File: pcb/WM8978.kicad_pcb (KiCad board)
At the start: 2 copper layers, 7.7 x 1.7 mm, 50 parts, among them CN2 HEADPHONE 3.5mm, SW4 RESET, U15 AMS1117-3.3, U16 WM8978GEFL/RV, U17 STM32F407VET6, X3 8MHz CL=12pF

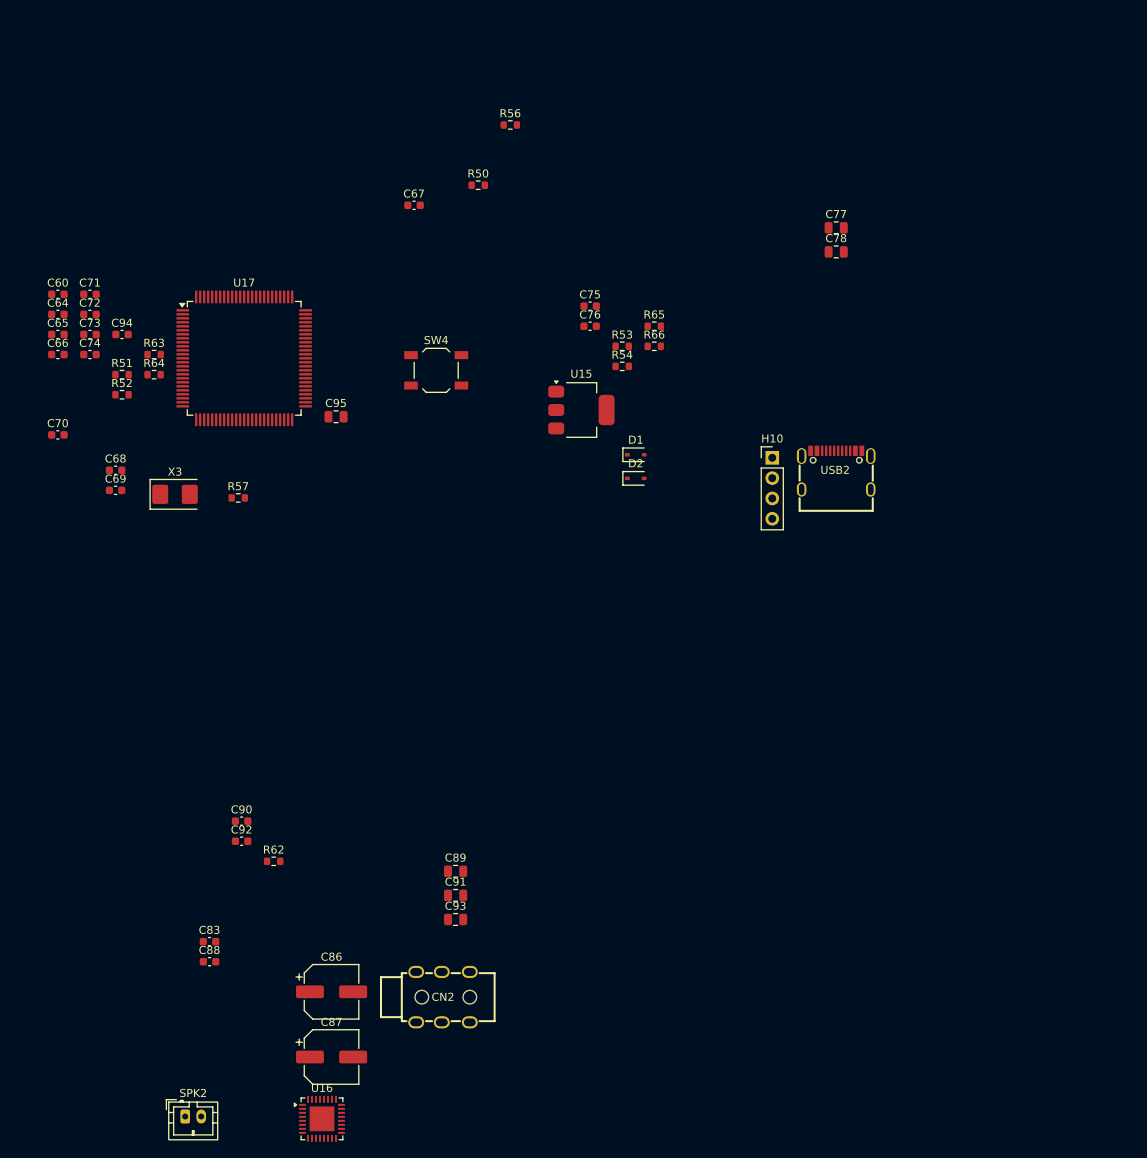
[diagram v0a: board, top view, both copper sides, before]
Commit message: 修复原理图电源网络并更新项目文档
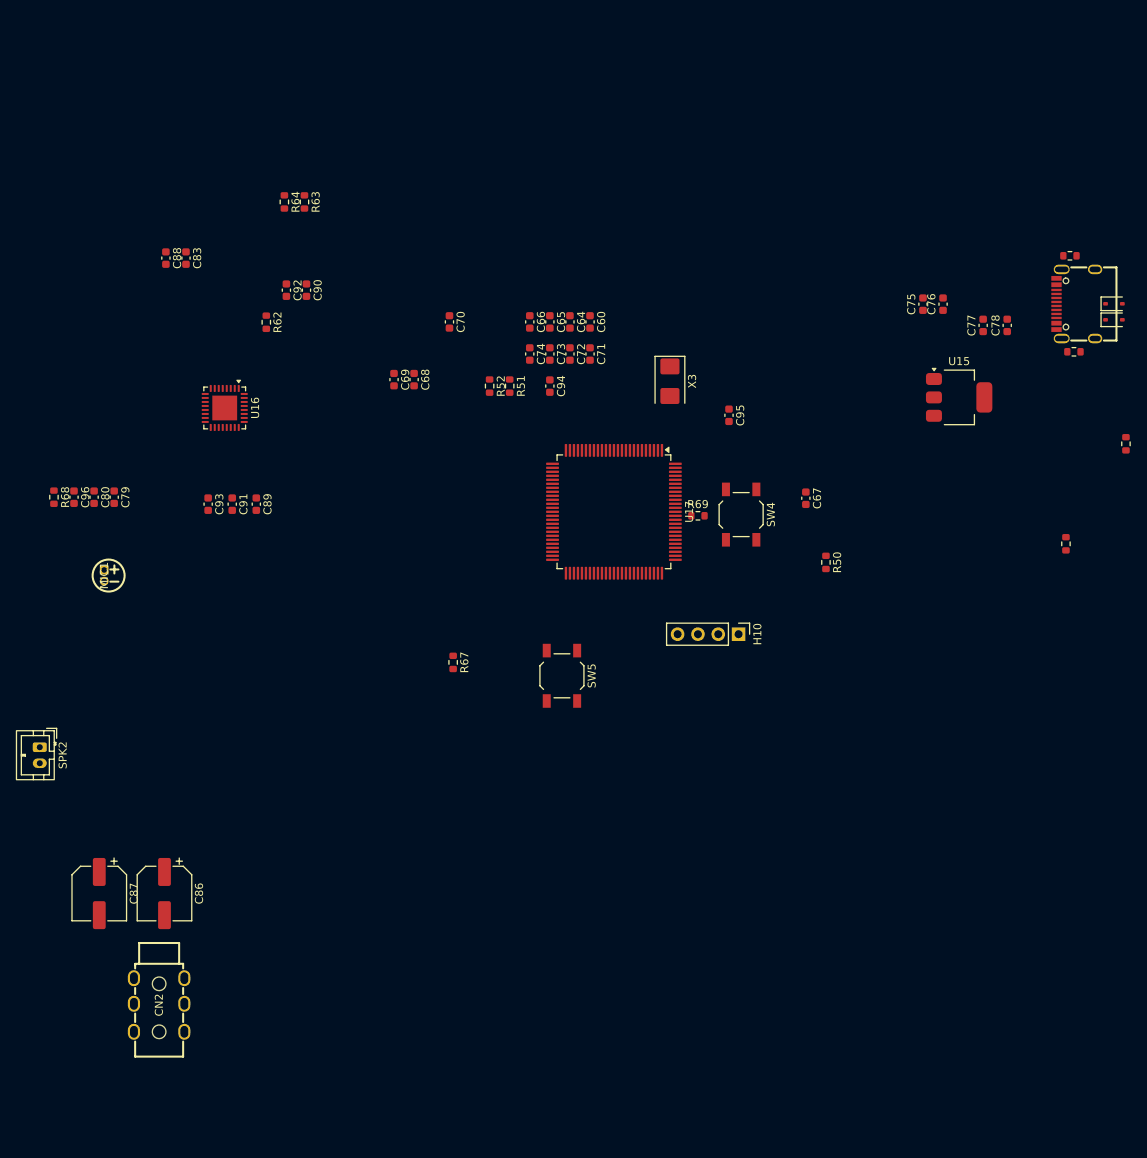
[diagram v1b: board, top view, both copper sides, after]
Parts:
- removed R56: 10k, Resistor_SMD:R_0603_1608Metric
- removed R57: 1M, Resistor_SMD:R_0603_1608Metric
- added C79: 1uF, Capacitor_SMD:C_0603_1608Metric, F.Cu at (90.0, 89.7)
- added C80: 1uF, Capacitor_SMD:C_0603_1608Metric, F.Cu at (87.5, 89.7)
- added C96: 4.7uF, Capacitor_SMD:C_0603_1608Metric, F.Cu at (85.0, 89.7)
- added MIC1: ELECTRET MIC, WM8978-import-fps:MIC-TH_BD4.0-P1.40-D0.4-L-FD, F.Cu at (88.8, 99.5)
- added R67: 1k, Resistor_SMD:R_0603_1608Metric, F.Cu at (132.4, 110.3)
- added R68: 2.2k, Resistor_SMD:R_0603_1608Metric, F.Cu at (82.5, 89.7)
- added R69: 10k, Resistor_SMD:R_0603_1608Metric, F.Cu at (163.0, 92.0)
- added SW5: BOOT, Button_Switch_SMD:SW_SPST_TL3342, F.Cu at (146.0, 112.0)
- C77, C89, C91, C93: value 10uF -> 4.7uF; footprint Capacitor_SMD:C_0805_2012Metric -> Capacitor_SMD:C_0603_1608Metric
- C78: footprint Capacitor_SMD:C_0805_2012Metric -> Capacitor_SMD:C_0603_1608Metric
- C86, C87: value 220uF/6.3V -> 220uF/16V
- C95: value 4.7uF -> 100nF; footprint Capacitor_SMD:C_0805_2012Metric -> Capacitor_SMD:C_0603_1608Metric
- U15: value AMS1117-3.3 -> TLV1117LV33DCYR
- moved U16 89.7 mm to (103.8, 78.5), turned to -90 degrees
- moved C88 88.1 mm to (96.5, 59.8), turned to -90 degrees
- moved C83 85.5 mm to (99.0, 59.8), turned to -90 degrees
- moved C92 69.1 mm to (111.6, 63.8), turned to -90 degrees
- moved R62 67.4 mm to (109.0, 67.8), turned to -90 degrees
- moved C90 66.9 mm to (114.1, 63.8), turned to -90 degrees
- moved C60 66.6 mm to (149.5, 67.8), turned to -90 degrees
- moved R53 64.1 mm to (216.5, 83.0), turned to 90 degrees
- moved R50 64.1 mm to (179.0, 97.8), turned to -90 degrees
- moved C64 64.0 mm to (147.0, 67.8), turned to -90 degrees
- moved X3 63.5 mm to (159.5, 75.2), turned to -90 degrees
- moved D2 63.0 mm to (215.0, 67.5)
- moved C71 63.0 mm to (149.5, 71.8), turned to -90 degrees
- moved D1 62.7 mm to (215.0, 65.5)
- moved C65 61.5 mm to (144.5, 67.8), turned to -90 degrees
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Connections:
- net /BOOT0 renamed Net-(U17A-BOOT0)
- net /CC1 renamed Net-(USB2-CC1)
- net /CC2 renamed Net-(USB2-CC2)
- net /LOUT2 renamed /SPK_N
- net /NRST renamed Net-(U17A-NRST)
- net /OS_IN renamed Net-(U17A-PH0-OSC_IN(PH0))
- net /OS_OUT renamed Net-(U17A-PH1-OSC_OUT(PH1))
- net /PA11 renamed /USB_DM
- net /PA12 renamed /USB_DP
- net /PA13 renamed Net-(U17A-PA13(JTMS-SWDIO))
- net /PA14 renamed Net-(U17A-PA14(JTCK-SWCLK))
- net /ROUT2 renamed /SPK_P
- net /USB_DM_CONN renamed Net-(D2-A1)
- net /USB_DP_CONN renamed Net-(D1-A1)
- net /VSSA renamed Net-(U17B-VSSA)
- net Net-(U16-MODE) renamed /MODE
- C60 pad 1: /VDDA -> /GND
- C60 pad 2: GND -> /VDDA
- C64 pad 1: GND -> /GND
- C65 pad 2: GND -> /GND
- C66 pad 2: GND -> /GND
- C67 pad 1: GND -> /GND
- C68 pad 2: GND -> /GND
- C69 pad 2: GND -> /GND
- C70 pad 1: VCC3V3 -> /3V3
- C70 pad 2: GND -> /GND
- C71 pad 1: VCC3V3 -> /3V3
- C71 pad 2: GND -> /GND
- C72 pad 1: VCC3V3 -> /3V3
- C72 pad 2: GND -> /GND
- C73 pad 1: VCC3V3 -> /3V3
- C73 pad 2: GND -> /GND
- C74 pad 1: VCC3V3 -> /3V3
- C74 pad 2: GND -> /GND
- C75 pad 1: GND -> /VBUS_5V
- C75 pad 2: +5V -> /GND
- C76 pad 1: GND -> /3V3
- C76 pad 2: VCC3V3 -> /GND
- C77 pad 1: GND -> /VBUS_5V
- C77 pad 2: +5V -> /GND
- C78 pad 1: GND -> /3V3
- C78 pad 2: VCC3V3 -> /GND
- C83 pad 1: GND -> /GND
- C86 pad 1: Net-(U16-ROUT1) -> /HP_L
- C87 pad 1: Net-(U16-LOUT1) -> /HP_R
- C88 pad 1: VCC3V3 -> /3V3
- C88 pad 2: GND -> /GND
- C89 pad 1: GND -> /GND
- C89 pad 2: VCC3V3 -> /3V3
- C90 pad 1: VCC3V3 -> /3V3
- C90 pad 2: GND -> /GND
- C91 pad 1: GND -> /GND
- C91 pad 2: VCC3V3 -> /3V3
- C92 pad 1: +5V -> /GND
- C92 pad 2: GND -> /VBUS_5V
- C93 pad 1: GND -> /VBUS_5V
- C93 pad 2: +5V -> /GND
- C94 pad 1: VCC3V3 -> /3V3
- C94 pad 2: GND -> /GND
- C95 pad 1: VCC3V3 -> /3V3
- C95 pad 2: GND -> /GND
- CN2 pad 2: GND -> /GND
- D1 pad 2: GND -> /GND
- D2 pad 2: GND -> /GND
- H10 pad 1: VCC3V3 -> /3V3
- H10 pad 4: GND -> /GND
- R50 pad 2: GND -> /GND
- R51 pad 2: GND -> /GND
- R52 pad 2: VCC3V3 -> /3V3
- R62 pad 1: GND -> /GND
- R63 pad 1: VCC3V3 -> Net-(U16-SDIN)
- R63 pad 2: /WM8978_SDIN -> /3V3
- R64 pad 1: VCC3V3 -> Net-(U16-SCLK)
- R64 pad 2: /WM8978_SCLK -> /3V3
- R65 pad 2: GND -> /GND
- R66 pad 2: GND -> /GND
- SW4 pad 2: GND -> /GND
- U15 pad 1: GND -> /GND
- U15 pad 2: VCC3V3 -> /3V3
- U15 pad 3: +5V -> /VBUS_5V
- U15 pad 4: VCC3V3 -> /3V3
- U16 pad 1: unconnected-(U16-LIP-Pad1) -> /MIC_LIP
- U16 pad 12: GND -> /GND
- U16 pad 13: VCC3V3 -> /GND
- U16 pad 14: VCC3V3 -> /3V3
- U16 pad 15: GND -> /GND
- U16 pad 16: /WM8978_SCLK -> Net-(U16-SCLK)
- U16 pad 17: /WM8978_SDIN -> Net-(U16-SDIN)
- U16 pad 2: unconnected-(U16-LIN-Pad2) -> /MIC_LIN
- U16 pad 24: GND -> /GND
- U16 pad 26: +5V -> /VBUS_5V
- U16 pad 28: GND -> /GND
- U16 pad 29: Net-(U16-ROUT1) -> /HP_R
- U16 pad 30: Net-(U16-LOUT1) -> /HP_L
- U16 pad 31: VCC3V3 -> /GND
- U16 pad 32: unconnected-(U16-MICBIAS-Pad32) -> Net-(U16-MICBIAS)
- U16 pad 33: GND -> /GND
- U16 pad 9: unconnected-(U16-ADCDAT-Pad9) -> /I2S_ADCDAT
- U17 pad 10: GND -> /GND
- U17 pad 100: VCC3V3 -> /3V3
- U17 pad 11: VCC3V3 -> /3V3
- U17 pad 17: unconnected-(U17A-PC2-Pad17) -> /I2S_ADCDAT
- U17 pad 19: VCC3V3 -> /3V3
- U17 pad 27: GND -> /GND
- U17 pad 28: VCC3V3 -> /3V3
- U17 pad 37: unconnected-(U17A-PB2-BOOT1(PB2)-Pad37) -> Net-(U17A-PB2-BOOT1(PB2))
- U17 pad 50: VCC3V3 -> /3V3
- U17 pad 6: VCC3V3 -> /3V3
- U17 pad 68: unconnected-(U17A-PA9-Pad68) -> Net-(U17A-PA9)
- U17 pad 74: GND -> /GND
- U17 pad 75: VCC3V3 -> /3V3
- U17 pad 87: /WM8978_SCLK -> /CODEC_SCLK
- U17 pad 88: /WM8978_SDIN -> /CODEC_SDIN
- U17 pad 99: GND -> /GND
- USB2 pad 1: GND -> /GND
- USB2 pad 2: GND -> /GND
- USB2 pad 3: GND -> /GND
- USB2 pad 4: GND -> /GND
- USB2 pad A1: GND -> /GND
- USB2 pad A12: GND -> /GND
- USB2 pad A4: +5V -> /VBUS_5V
- USB2 pad A9: +5V -> /VBUS_5V
- USB2 pad B1: GND -> /GND
- USB2 pad B12: GND -> /GND
- USB2 pad B4: +5V -> /VBUS_5V
- USB2 pad B9: +5V -> /VBUS_5V
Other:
- board size 7.7 x 1.7 mm -> 1.7 x 7.7 mm

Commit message: 更新单页原理图布局并同步 PCB
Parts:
- C95: value 100nF -> 4.7uF
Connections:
- C79 pad 1: Net-(C79-Pad1) -> /MIC_LIP
- C79 pad 2: /MIC_LIP -> Net-(C79-Pad2)
- C80 pad 1: /GND -> unconnected-(C80-Pad1)
- C80 pad 2: /MIC_LIN -> unconnected-(C80-Pad2)
- C83 pad 1: /GND -> unconnected-(C83-Pad1)
- C83 pad 2: Net-(U16-VMID) -> unconnected-(C83-Pad2)
- C89 pad 1: /GND -> unconnected-(C89-Pad1)
- C89 pad 2: /3V3 -> unconnected-(C89-Pad2)
- C91 pad 1: /GND -> unconnected-(C91-Pad1)
- C91 pad 2: /3V3 -> unconnected-(C91-Pad2)
- C93 pad 1: /VBUS_5V -> unconnected-(C93-Pad1)
- C93 pad 2: /GND -> unconnected-(C93-Pad2)
- C96 pad 1: /GND -> unconnected-(C96-Pad1)
- C96 pad 2: Net-(U16-MICBIAS) -> unconnected-(C96-Pad2)
- MIC1 pad 1: Net-(C79-Pad1) -> Net-(C79-Pad2)
- R68 pad 2: Net-(C79-Pad1) -> Net-(C79-Pad2)
- U16 pad 13: /GND -> /3V3
- U16 pad 27: Net-(U16-VMID) -> unconnected-(U16-VMID-Pad27)
- U16 pad 31: /GND -> /3V3
- U16 pad 32: Net-(U16-MICBIAS) -> unconnected-(U16-MICBIAS-Pad32)

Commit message: 9.22
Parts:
- removed C60, C67, C70, C71, C72, C73, C74, C94: 100nF, Capacitor_SMD:C_0603_1608Metric
- removed C64: 1uF, Capacitor_SMD:C_0603_1608Metric
- removed C65, C66: 2.2uF, Capacitor_SMD:C_0603_1608Metric
- removed C68, C69: 18pF, Capacitor_SMD:C_0603_1608Metric
- removed C95: 4.7uF, Capacitor_SMD:C_0603_1608Metric
- removed H10: SWD 1x4, Connector_PinHeader_2.54mm:PinHeader_1x04_P2.54mm_Vertical
- removed R50, R69: 10k, Resistor_SMD:R_0603_1608Metric
- removed R51, R52: 0R, Resistor_SMD:R_0603_1608Metric
- removed R67: 1k, Resistor_SMD:R_0603_1608Metric
- removed SW4: RESET, Button_Switch_SMD:SW_SPST_TL3342
- removed SW5: BOOT, Button_Switch_SMD:SW_SPST_TL3342
- removed X3: 8MHz CL=12pF, Crystal:Crystal_SMD_5032-2Pin_5.0x3.2mm
- added C100: 10uF / 16V, Capacitor_SMD:C_0603_1608Metric, F.Cu at (135.5, 64.7)
- added C101: 1uF / 16V, Capacitor_SMD:C_0603_1608Metric, F.Cu at (122.0, 60.5)
- added C102: 100nF, Capacitor_SMD:C_0603_1608Metric, F.Cu at (121.5, 58.0)
- added C103: 10nF, Capacitor_SMD:C_0603_1608Metric, F.Cu at (141.5, 54.5)
- added C104: 100nF, Capacitor_SMD:C_0603_1608Metric, F.Cu at (159.0, 73.4)
- added C105: 1uF, Capacitor_SMD:C_0603_1608Metric, F.Cu at (159.0, 75.9)
- added C106: 100nF, Capacitor_SMD:C_0603_1608Metric, F.Cu at (159.0, 78.4)
- added C107: 4.7uF, Capacitor_SMD:C_0603_1608Metric, F.Cu at (159.0, 80.9)
- added C97: 100nF, Capacitor_SMD:C_0603_1608Metric, F.Cu at (122.0, 63.5)
- added C98: 10uF / 16V, Capacitor_SMD:C_0603_1608Metric, F.Cu at (120.5, 63.5)
- added C99: 100nF, Capacitor_SMD:C_0603_1608Metric, F.Cu at (137.0, 64.7)
- added J2: JLINK SWD, Connector_JST:JST_XH_B4B-XH-A_1x04_P2.50mm_Vertical, F.Cu at (115.0, 60.0)
- added R70: 10k, Resistor_SMD:R_0603_1608Metric, F.Cu at (121.5, 56.5)
- added R71: 1k, Resistor_SMD:R_0603_1608Metric, F.Cu at (119.0, 62.5)
- added R72: 330R, Resistor_SMD:R_0603_1608Metric, F.Cu at (121.5, 55.0)
- added R73: 33R, Resistor_SMD:R_0603_1608Metric, F.Cu at (135.5, 59.0)
- added R74: 100k, Resistor_SMD:R_0603_1608Metric, F.Cu at (129.7, 54.0)
- added R75: 33R, Resistor_SMD:R_0603_1608Metric, F.Cu at (159.0, 83.4)
- added R76: 33R, Resistor_SMD:R_0603_1608Metric, F.Cu at (163.0, 73.4)
- added R77: 0R, Resistor_SMD:R_0603_1608Metric, F.Cu at (163.0, 75.9)
- added R78: 61.9k, Resistor_SMD:R_0603_1608Metric, F.Cu at (163.0, 78.4)
- added R79: 100k, Resistor_SMD:R_0603_1608Metric, F.Cu at (163.0, 80.9)
- added R80: 100k, Resistor_SMD:R_0603_1608Metric, F.Cu at (163.0, 83.4)
- added SW1: RESET, Button_Switch_SMD:SW_Tactile_SPST_NO_Straight_CK_PTS636Sx25SMTRLFS, F.Cu at (114.5, 54.5)
- added TP1: RESET, TestPoint:TestPoint_Pad_D1.0mm, F.Cu at (158.5, 64.5)
- added TP10: SDA, TestPoint:TestPoint_Pad_D1.0mm, F.Cu at (167.7, 64.5)
- added TP11: SCL, TestPoint:TestPoint_Pad_D1.0mm, F.Cu at (167.7, 67.6)
- added TP12: FAULT, TestPoint:TestPoint_Pad_D1.0mm, F.Cu at (167.7, 70.6)
- added TP2: GND, TestPoint:TestPoint_Pad_D1.0mm, F.Cu at (158.5, 67.6)
- added TP3: RAW 5V, TestPoint:TestPoint_Pad_D1.0mm, F.Cu at (158.5, 70.6)
- added TP4: 5V, TestPoint:TestPoint_Pad_D1.0mm, F.Cu at (161.6, 64.5)
- added TP5: 3V3, TestPoint:TestPoint_Pad_D1.0mm, F.Cu at (161.6, 67.6)
- added TP6: CORE, TestPoint:TestPoint_Pad_D1.0mm, F.Cu at (161.6, 70.6)
- added TP7: MCLK, TestPoint:TestPoint_Pad_D1.0mm, F.Cu at (164.6, 64.5)
- added TP8: BCLK, TestPoint:TestPoint_Pad_D1.0mm, F.Cu at (164.6, 67.6)
- added TP9: LRCLK, TestPoint:TestPoint_Pad_D1.0mm, F.Cu at (164.6, 70.6)
- added U1: ATSAMD21E18A-A, Package_QFP:TQFP-32_7x7mm_P0.8mm, F.Cu at (128.5, 61.0)
- added U18: SN74LVC1G125DBVR, Package_TO_SOT_SMD:SOT-23-5, F.Cu at (167.6, 79.2)
- added Y1: 12MHz / 3.3V / 50ppm, Oscillator:Oscillator_SMD_Abracon_ASE-4Pin_3.2x2.5mm, F.Cu at (139.5, 58.0)
- C86, C87: value 220uF/16V -> 470uF/16V; footprint Capacitor_SMD:CP_Elec_6.3x5.8 -> Capacitor_SMD:CP_Elec_8x10.5
- U16: value WM8978GEFL/RV -> WM8978CGEFL/RV; footprint Package_DFN_QFN:QFN-32-1EP_5x5mm_P0.5mm_EP3.1x3.1mm -> Package_DFN_QFN:QFN-32-1EP_5x5mm_P0.5mm_EP3.45x3.45mm
- U17: value STM32F407VET6 -> TPS2553DBVR; footprint Package_QFP:LQFP-100_14x14mm_P0.5mm -> Package_TO_SOT_SMD:SOT-23-6
- moved R53 96.8 mm to (125.0, 51.5), turned to -90 degrees
- moved D1 93.7 mm to (122.5, 50.5), turned to 180 degrees
- moved R54 93.1 mm to (127.0, 51.5), turned to -90 degrees
- moved R66 90.5 mm to (120.0, 46.0), turned to -90 degrees
- moved D2 87.2 mm to (129.5, 50.5)
- moved USB2 86.5 mm to (126.1, 45.6), turned to 180 degrees
- moved R65 82.1 mm to (132.0, 46.0), turned to -90 degrees
- moved C88 80.5 mm to (165.0, 102.0), turned to 90 degrees
- moved C80 73.5 mm to (160.0, 102.0), turned to 90 degrees
- moved C87 71.8 mm to (134.0, 84.0)
- moved CN2 66.6 mm to (130.3, 96.3), turned to 90 degrees
- moved U15 65.5 mm to (137.5, 47.0)
- moved C77 65.2 mm to (135.2, 53.0), turned to 0 degrees
- moved C86 62.9 mm to (126.5, 84.0)
- moved C78 62.4 mm to (141.5, 51.5), turned to 0 degrees
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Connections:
- net /SPK_N renamed Net-(U16-LOUT2)
- net /SPK_P renamed Net-(U16-ROUT2)
- net Net-(U16-SCLK) renamed /CODEC_SCL
- net Net-(U16-SDIN) renamed /CODEC_SDA
- C75 pad 2: /GND -> GND
- C76 pad 1: /3V3 -> +3V3
- C76 pad 2: /GND -> GND
- C77 pad 2: /GND -> GND
- C78 pad 1: /3V3 -> +3V3
- C78 pad 2: /GND -> GND
- C80 pad 1: unconnected-(C80-Pad1) -> /MIC_LIN
- C80 pad 2: unconnected-(C80-Pad2) -> GND
- C83 pad 1: unconnected-(C83-Pad1) -> Net-(U16-VMID)
- C83 pad 2: unconnected-(C83-Pad2) -> GND
- C86 pad 1: /HP_L -> Net-(U16-ROUT1)
- C87 pad 1: /HP_R -> Net-(U16-LOUT1)
- C88 pad 1: /3V3 -> +3V3
- C88 pad 2: /GND -> GND
- C89 pad 1: unconnected-(C89-Pad1) -> +3V3
- C89 pad 2: unconnected-(C89-Pad2) -> GND
- C90 pad 1: /3V3 -> +3V3
- C90 pad 2: /GND -> GND
- C91 pad 1: unconnected-(C91-Pad1) -> +3V3
- C91 pad 2: unconnected-(C91-Pad2) -> GND
- C92 pad 1: /GND -> GND
- C93 pad 1: unconnected-(C93-Pad1) -> GND
- C93 pad 2: unconnected-(C93-Pad2) -> /VBUS_5V
- C96 pad 1: unconnected-(C96-Pad1) -> /MICBIAS
- C96 pad 2: unconnected-(C96-Pad2) -> GND
- CN2 pad 2: /GND -> GND
- D1 pad 2: /GND -> GND
- D2 pad 2: /GND -> GND
- MIC1 pad 2: /GND -> GND
- R62 pad 1: /GND -> GND
- R63 pad 2: /3V3 -> +3V3
- R64 pad 2: /3V3 -> +3V3
- R65 pad 2: /GND -> GND
- R66 pad 2: /GND -> GND
- U15 pad 1: /GND -> GND
- U15 pad 2: /3V3 -> +3V3
- U15 pad 4: /3V3 -> +3V3
- U16 pad 12: /GND -> GND
- U16 pad 13: /3V3 -> +3V3
- U16 pad 14: /3V3 -> +3V3
- U16 pad 15: /GND -> GND
- U16 pad 24: /GND -> GND
- U16 pad 27: unconnected-(U16-VMID-Pad27) -> Net-(U16-VMID)
- U16 pad 28: /GND -> GND
- U16 pad 29: /HP_R -> Net-(U16-ROUT1)
- U16 pad 30: /HP_L -> Net-(U16-LOUT1)
- U16 pad 31: /3V3 -> /AVDD_3V3
- U16 pad 32: unconnected-(U16-MICBIAS-Pad32) -> /MICBIAS
- U16 pad 33: /GND -> GND
- U16 pad 7: /I2S_LRCLK -> /CODEC_LRCLK
- U16 pad 8: /I2S_BCLK -> /CODEC_BCLK
- U17 pad 1: unconnected-(U17A-PE2-Pad1) -> /VBUS_RAW
- U17 pad 2: unconnected-(U17A-PE3-Pad2) -> GND
- U17 pad 3: unconnected-(U17A-PE4-Pad3) -> /VBUS_RAW
- U17 pad 4: unconnected-(U17A-PE5-Pad4) -> Net-(U17-~{FAULT})
- U17 pad 5: unconnected-(U17A-PE6-Pad5) -> Net-(U17-ILIM)
- U17 pad 6: /3V3 -> /VBUS_5V
- USB2 pad 1: /GND -> GND
- USB2 pad 2: /GND -> GND
- USB2 pad 3: /GND -> GND
- USB2 pad 4: /GND -> GND
- USB2 pad A1: /GND -> GND
- USB2 pad A12: /GND -> GND
- USB2 pad A4: /VBUS_5V -> /VBUS_RAW
- USB2 pad A9: /VBUS_5V -> /VBUS_RAW
- USB2 pad B1: /GND -> GND
- USB2 pad B12: /GND -> GND
- USB2 pad B4: /VBUS_5V -> /VBUS_RAW
- USB2 pad B9: /VBUS_5V -> /VBUS_RAW
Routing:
- net +3V3: track 0.00 -> 61.5 mm
- net /VBUS_5V: track 0.00 -> 23.6 mm
- net /SWDIO: track 0.00 -> 16.4 mm
- net /AUDIO_CLK_EN: track 0.00 -> 15.1 mm
- net /SWCLK: track 0.00 -> 10.3 mm
- net Net-(D2-A1): track 0.00 -> 7.25 mm
- net Net-(D1-A1): track 0.00 -> 7.23 mm
- net Net-(USB2-CC1): track 0.00 -> 6.46 mm
- net Net-(USB2-CC2): track 0.00 -> 6.13 mm
- net /MCU_RESET_N: track 0.00 -> 5.50 mm
- net /USB_DP: track 0.00 -> 4.80 mm
- net /USB_DM: track 0.00 -> 4.72 mm
- net /CODEC_SCL: track 0.00 -> 3.82 mm
- net Net-(R72-Pad2): track 0.00 -> 2.51 mm
- net /VDDCORE: track 0.00 -> 2.39 mm
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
